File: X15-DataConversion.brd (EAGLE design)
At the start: 24.3 x 25.4 mm, 25 parts, among them Y1 ECS-80-18-4X

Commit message: layout mostly done
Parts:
- moved R2 2.31 mm to (14.4, 18.2), flipped to the top, turned to 0 degrees
- moved R9 2.26 mm to (20.6, 10.8), turned to 270 degrees
- moved R3 0.89 mm to (14.4, 16.5), flipped to the top, turned to 0 degrees
- moved D3 0.88 mm to (3.72, 4.92)
- moved Y1 0.71 mm to (21.1, 18.6)
- moved R8 0.70 mm to (19.0, 10.8), turned to 270 degrees
- moved C8 0.62 mm to (21.1, 18.5)
- moved C7 0.52 mm to (19.6, 18.6)
- moved R1 0.50 mm to (18.3, 5.04)
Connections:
- net 3.3V renamed 3V3
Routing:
- net ALERT2: track 0.00 -> 37.9 mm, vias 0 -> 1
- net NRST: track 10.8 -> 46.9 mm, vias 0 -> 2
- net ALERT1: track 0.00 -> 33.9 mm, vias 0 -> 1
- net C2_2: track 0.00 -> 18.4 mm, vias 0 -> 3
- net CAN_L: track 6.06 -> 23.0 mm
- net C2_1: track 0.00 -> 15.3 mm, vias 0 -> 1
- net SWCLK: track 8.59 -> 23.6 mm, vias 0 -> 1
- net 3V3: track 51.3 -> 64.2 mm, vias 2 -> 3
- net N$4: track 11.0 -> 6.22 mm
- net N$6: track 0.00 -> 4.75 mm
- net N$7: track 0.00 -> 2.99 mm
- net GND: track 0.00 -> 2.83 mm, vias 0 -> 8
- net OSC_IN: track 2.28 -> 4.44 mm
- net N$3: track 14.4 -> 13.2 mm
- net OSC_OUT: track 2.87 -> 1.99 mm
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
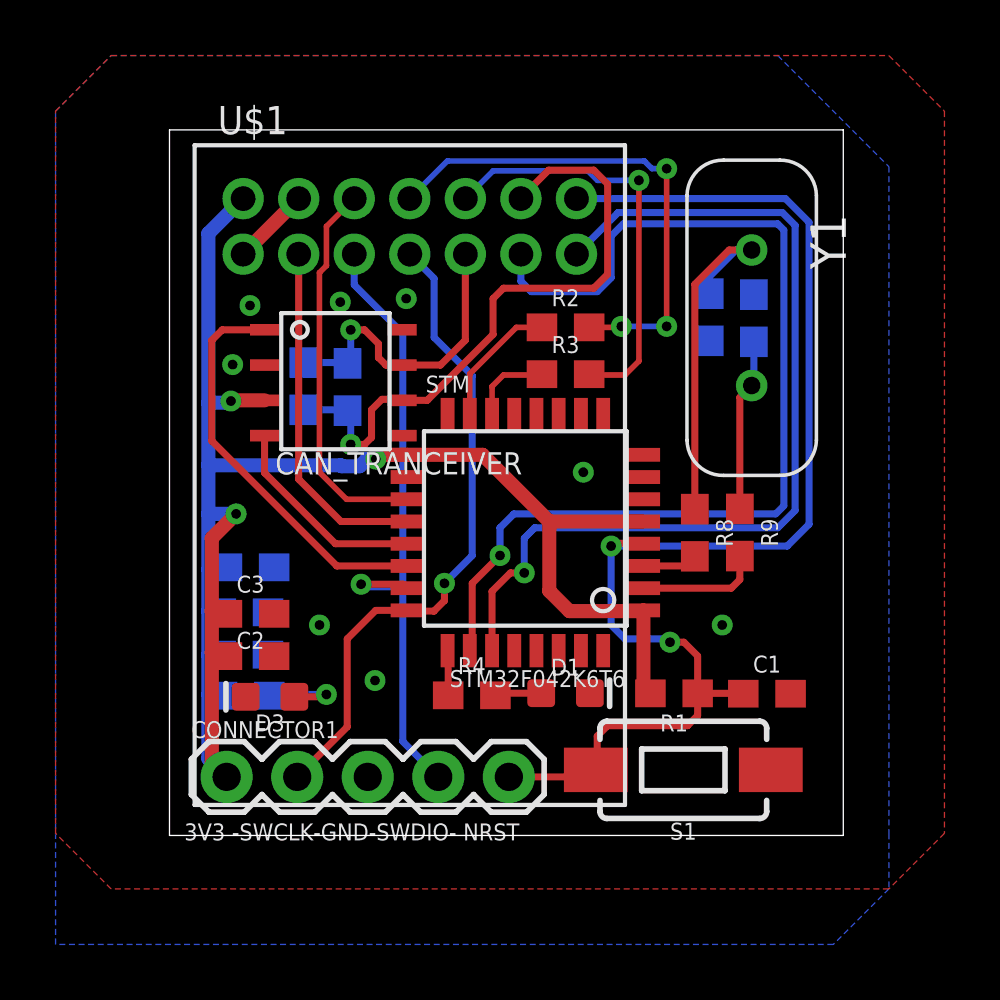
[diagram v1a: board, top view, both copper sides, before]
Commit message: fixing board layout
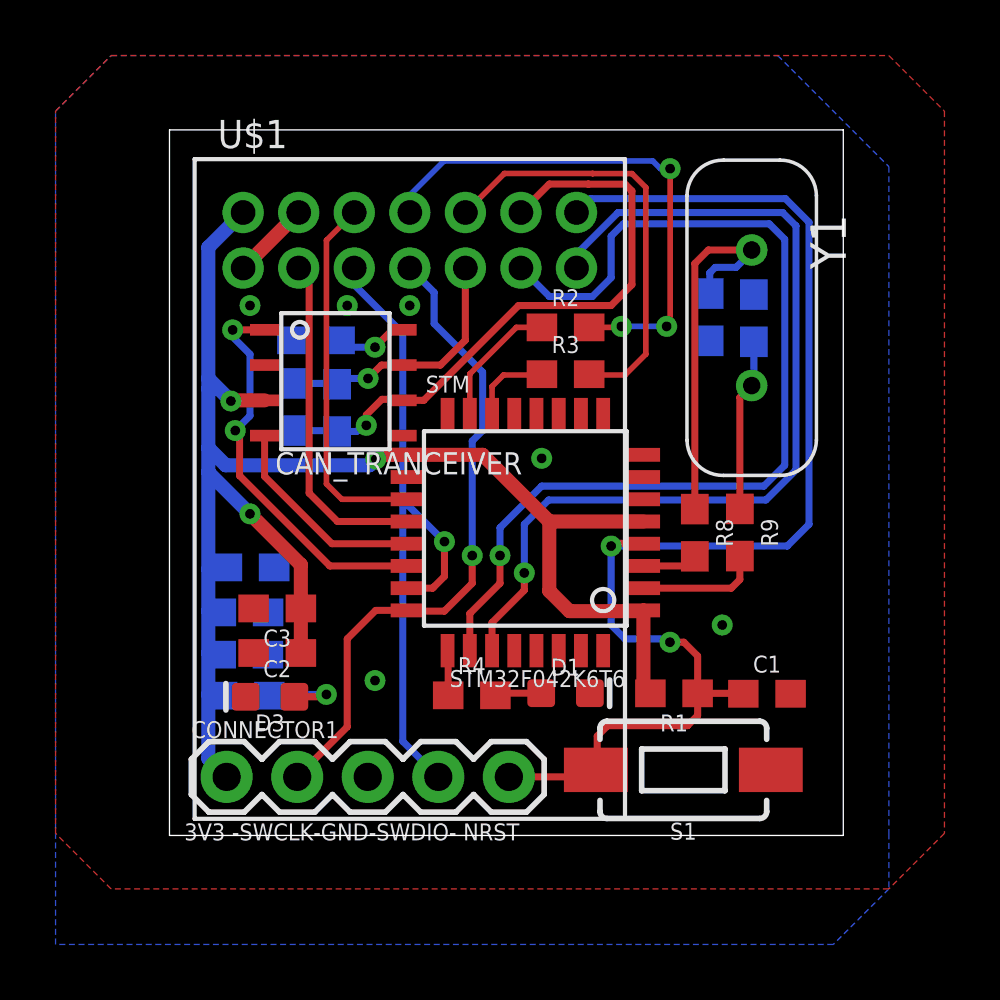
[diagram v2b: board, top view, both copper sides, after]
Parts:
- added R10: 30k, SparkFun-Resistors:0603
- moved C3 0.98 mm to (3.98, 8.10), turned to 180 degrees
- moved C2 0.97 mm to (3.98, 6.49), turned to 180 degrees
- moved R6 0.84 mm to (6.14, 15.3)
- moved R7 0.79 mm to (4.67, 15.3)
- moved U$1 0.50 mm to (8.75, 21.4)
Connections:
- new net N$2: CAN_TRANCEIVER.RS, R10.1
- net GND: now also R10.2; no longer CAN_TRANCEIVER.RS
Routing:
- net 3V3: track 64.2 -> 59.9 mm
- net N$2: track 0.00 -> 2.61 mm, vias 0 -> 1
- net CAN_H: track 11.3 -> 9.35 mm
- net ALERT2: track 37.9 -> 36.3 mm
- net SWDIO: track 23.4 -> 24.5 mm
- net C2_2: track 18.4 -> 19.2 mm
- net CLK: track 13.9 -> 13.3 mm
- net CAN_L: track 23.0 -> 22.5 mm
- net N$3: track 13.2 -> 13.7 mm
- net C2_1: track 15.3 -> 15.7 mm, vias 1 -> 0
- net CAN_TX: track 14.6 -> 14.5 mm, vias 0 -> 2
- net GND: vias 8 -> 6

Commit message: made can lines sameish length
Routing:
- net CAN_H: track 9.35 -> 20.3 mm
- net CAN_RX: track 7.61 -> 16.6 mm
- net SWDIO: track 24.5 -> 22.1 mm
- net 3V3: track 59.9 -> 61.7 mm
- net C2_2: track 19.2 -> 18.2 mm, vias 3 -> 2
- net GND: vias 6 -> 5

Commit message: cleaning up board layout
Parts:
- moved R2 0.45 mm to (14.7, 18.0)
- moved R3 0.40 mm to (14.7, 16.4)
- moved D3 0.26 mm to (3.97, 4.96)
- moved C4 0.22 mm to (2.79, 9.57)
- moved C3 0.18 mm to (3.82, 8.03)
- moved C2 0.17 mm to (3.82, 6.46)
- moved C5 0.07 mm to (2.79, 8.03)
- moved R5 0.05 mm to (2.79, 4.96)
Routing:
- net CAN_RX: track 16.6 -> 14.1 mm
- net CAN_H: track 20.3 -> 21.5 mm
- net 3V3: track 61.7 -> 62.8 mm
- net GND: vias 5 -> 6
